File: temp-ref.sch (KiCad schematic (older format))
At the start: 37 parts, among them IC1 INA211AIDCKT, IC2 INA211AIDCKT, J1 Conn_01x05_Male, J2 USB_C_Receptacle_USB2.0, Q1 Q_NMOS_GDS, Q3 Q_NMOS_GDS, SW1 SW_SPST, SW2 SW_SPST, SW3 SW_SPST, SW4 SW_SPST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

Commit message: layout attempt 1
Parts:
- removed U6: adafruit-tft-120x135-4383, temp-ref:adafruit-tft-4383, symbol adafruit-tft-120x135-4383:adafruit-tft-120x135-4383
- added Q2: MMBT3904, Package_TO_SOT_SMD:SOT-23, symbol Transistor_BJT:MMBT3904
- added R3, R5: 10k, Resistor_SMD:R_0603_1608Metric, symbol Device:R_Small
- added R9: 33, Resistor_SMD:R_0603_1608Metric, symbol Device:R_Small
- added U6: spi-tft-1.14-240x135, temp-ref:TFT-1.14-240-135, symbol spi-tft-1.14:spi-tft-1.14-240x135
- J2: footprint Connector_USB:USB_C_Receptacle_JAE_DX07S024WJ3R400 -> Connector_USB:USB_C_Receptacle_Amphenol_12401610E4-2A
- SW1, SW2, SW3, SW4: footprint Button_Switch_SMD:SW_Push_1P1T_NO_CK_KSC7xxJ -> temp-ref:5.2mm_Tact_reverse_mount
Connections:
- net labels removed: DISP_MISO, DISP_SDCS
- wire segments 216 -> 231
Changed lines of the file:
@@
 F 0 "J2" H 6557 5367 50  0000 C CNN
 F 1 "USB_C_Receptacle_USB2.0" H 6557 5276 50  0000 C CNN
-F 2 "Connector_USB:USB_C_Receptacle_JAE_DX07S024WJ3R400" H 6600 4500 50  0001 C CNN
+F 2 "Connector_USB:USB_C_Receptacle_Amphenol_12401610E4-2A" H 6600 4500 50  0001 C CNN
 F 3 "https://www.usb.org/sites/default/files/documents/usb_type-c.zip" H 6600 4500 50  0001 C CNN
 	1    6450 4500
@@
 F 0 "SW1" H 7150 2485 50  0000 C CNN
 F 1 "SW_SPST" H 7150 2394 50  0000 C CNN
-F 2 "Button_Switch_SMD:SW_Push_1P1T_NO_CK_KSC7xxJ" H 7150 2250 50  0001 C CNN
+F 2 "temp-ref:5.2mm_Tact_reverse_mount" H 7150 2250 50  0001 C CNN
 F 3 "~" H 7150 2250 50  0001 C CNN
 	1    7150 2250
@@
 F 0 "SW2" H 7150 2935 50  0000 C CNN
 F 1 "SW_SPST" H 7150 2844 50  0000 C CNN
-F 2 "Button_Switch_SMD:SW_Push_1P1T_NO_CK_KSC7xxJ" H 7150 2700 50  0001 C CNN
+F 2 "temp-ref:5.2mm_Tact_reverse_mount" H 7150 2700 50  0001 C CNN
 F 3 "~" H 7150 2700 50  0001 C CNN
 	1    7150 2700
@@
 F 0 "SW3" H 7150 3335 50  0000 C CNN
 F 1 "SW_SPST" H 7150 3244 50  0000 C CNN
-F 2 "Button_Switch_SMD:SW_Push_1P1T_NO_CK_KSC7xxJ" H 7150 3100 50  0001 C CNN
+F 2 "temp-ref:5.2mm_Tact_reverse_mount" H 7150 3100 50  0001 C CNN
 F 3 "~" H 7150 3100 50  0001 C CNN
 	1    7150 3100
@@
 F 0 "SW4" H 7150 3585 50  0000 C CNN
 F 1 "SW_SPST" H 7150 3494 50  0000 C CNN
-F 2 "Button_Switch_SMD:SW_Push_1P1T_NO_CK_KSC7xxJ" H 7150 3350 50  0001 C CNN
+F 2 "temp-ref:5.2mm_Tact_reverse_mount" H 7150 3350 50  0001 C CNN
 F 3 "~" H 7150 3350 50  0001 C CNN
 	1    7150 3350
@@
 Text GLabel 1500 2000 0    50   Input ~ 0
 HEATER1
-Text GLabel 1500 3000 0    50   Input ~ 0
+Text GLabel 1500 2500 0    50   Input ~ 0
 WIFI_G0
-Text GLabel 1500 3100 0    50   Input ~ 0
+Text GLabel 1500 1800 0    50   Input ~ 0
 WIFI_G2
 Text GLabel 1500 2300 0    50   Input ~ 0
 WIFI_TX
-Text GLabel 1500 2900 0    50   Input ~ 0
+Text GLabel 1500 1700 0    50   Input ~ 0
 WIFI_RST
 Text GLabel 6800 2250 0    50   Input ~ 0
@@
 L power:+3V3 #PWR0149
 U 1 1 5EB7C07B
-P 4650 4500
-F 0 "#PWR0149" H 4650 4350 50  0001 C CNN
-F 1 "+3V3" H 4665 4673 50  0000 C CNN
-F 2 "" H 4650 4500 50  0001 C CNN
-F 3 "" H 4650 4500 50  0001 C CNN
-	1    4650 4500
-	0    -1   -1   0
-$EndComp
-Wire Wire Line
-	4800 4500 4650 4500
+P 4850 5950
+F 0 "#PWR0149" H 4850 5800 50  0001 C CNN
+F 1 "+3V3" H 4865 6123 50  0000 C CNN
+F 2 "" H 4850 5950 50  0001 C CNN
+F 3 "" H 4850 5950 50  0001 C CNN
+	1    4850 5950
+	0    -1   -1   0
+$EndComp
 $Comp
 L power:GND #PWR0150
 U 1 1 5EB87206
-P 4700 4700
-F 0 "#PWR0150" H 4700 4450 50  0001 C CNN
-F 1 "GND" H 4705 4527 50  0000 C CNN
-F 2 "" H 4700 4700 50  0001 C CNN
-F 3 "" H 4700 4700 50  0001 C CNN
-	1    4700 4700
+P 4800 6850
+F 0 "#PWR0150" H 4800 6600 50  0001 C CNN
+F 1 "GND" H 4805 6677 50  0000 C CNN
+F 2 "" H 4800 6850 50  0001 C CNN
+F 3 "" H 4800 6850 50  0001 C CNN
+	1    4800 6850
 	0    1    1    0
 $EndComp
-Wire Wire Line
-	4800 4700 4700 4700
-Text GLabel 4450 4800 0    50   Input ~ 0
+Text GLabel 4850 6450 0    50   Input ~ 0
 DISP_SCK
-Text GLabel 4450 4900 0    50   Input ~ 0
-DISP_MISO
-Text GLabel 4450 5000 0    50   Input ~ 0
+Text GLabel 4850 6350 0    50   Input ~ 0
 DISP_MOSI
-Text GLabel 4450 5100 0    50   Input ~ 0
+Text GLabel 4850 6550 0    50   Input ~ 0
 DISP_CS
-Text GLabel 4450 5200 0    50   Input ~ 0
+Text GLabel 4850 6150 0    50   Input ~ 0
 DISP_RST
-Text GLabel 4450 5300 0    50   Input ~ 0
+Text GLabel 4850 6250 0    50   Input ~ 0
 DISP_DC
-Text GLabel 4450 5400 0    50   Input ~ 0
-DISP_SDCS
-Text GLabel 4450 5500 0    50   Input ~ 0
+Text GLabel 3000 6350 0    50   Input ~ 0
 DISP_BACKLIGHT
-Wire Wire Line
-	4800 4800 4450 4800
-Wire Wire Line
-	4800 4900 4450 4900
-Wire Wire Line
-	4800 5000 4450 5000
-Wire Wire Line
-	4800 5100 4450 5100
-Wire Wire Line
-	4800 5200 4450 5200
-Wire Wire Line
-	4800 5300 4450 5300
-Wire Wire Line
-	4800 5400 4450 5400
-Wire Wire Line
-	4800 5500 4450 5500
 Text GLabel 1500 2400 0    50   Input ~ 0
 WIFI_RX
@@
 Text GLabel 3650 1700 2    50   Input ~ 0
 DISP_SCK
-Text GLabel 1500 2500 0    50   Input ~ 0
-DISP_MISO
 Text GLabel 3650 1800 2    50   Input ~ 0
 DISP_MOSI
@@
 Text GLabel 1500 4000 0    50   Input ~ 0
 DISP_DC
-Text GLabel 1500 1800 0    50   Input ~ 0
-DISP_SDCS
 Text GLabel 1500 2800 0    50   Input ~ 0
 DISP_BACKLIGHT
@@
 	9900 9300 9850 9300
 $Comp
-L adafruit-tft-120x135-4383:adafruit-tft-120x135-4383 U6
-U 1 1 5F0AA818
-P 4950 5800
-F 0 "U6" H 5228 6671 50  0000 L CNN
-F 1 "adafruit-tft-120x135-4383" H 5228 6580 50  0000 L CNN
-F 2 "temp-ref:adafruit-tft-4383" H 4950 5800 50  0001 C CNN
-F 3 "" H 4950 5800 50  0001 C CNN
-	1    4950 5800
-	1    0    0    -1
-$EndComp
-$Comp
 L STS-30-DIS:STS-30-DIS U5
 U 1 1 5F0AB74B
@@
 	0    -1   1    0
 $EndComp
+$Comp
+L spi-tft-1.14:spi-tft-1.14-240x135 U6
+U 1 1 5EAE6EF2
+P 5150 6750
+F 0 "U6" H 5378 7146 50  0000 L CNN
+F 1 "spi-tft-1.14-240x135" H 5378 7055 50  0000 L CNN
+F 2 "temp-ref:TFT-1.14-240-135" H 5250 6250 50  0001 C CNN
+F 3 "" H 5250 6250 50  0001 C CNN
+	1    5150 6750
+	1    0    0    -1
+$EndComp
+$Comp
+L Transistor_BJT:MMBT3904 Q2
+U 1 1 5EA5FD70
+P 3850 6350
+F 0 "Q2" H 4041 6396 50  0000 L CNN
+F 1 "MMBT3904" H 3500 6500 50  0000 L CNN
+F 2 "Package_TO_SOT_SMD:SOT-23" H 4050 6275 50  0001 L CIN
+F 3 "https://www.fairchildsemi.com/datasheets/2N/2N3904.pdf" H 3850 6350 50  0001 L CNN
+	1    3850 6350
+	1    0    0    -1
+$EndComp
+$Comp
+L Device:R_Small R5
+U 1 1 5EA60C2A
+P 3400 6350
+F 0 "R5" V 3350 6200 50  0000 C CNN
+F 1 "10k" V 3400 6350 39  0000 C CNN
+F 2 "Resistor_SMD:R_0603_1608Metric" H 3400 6350 50  0001 C CNN
+F 3 "~" H 3400 6350 50  0001 C CNN
+	1    3400 6350
+	0    -1   -1   0
+$EndComp
+$Comp
+L Device:R_Small R3
+U 1 1 5EA615A5
+P 3200 6150
+F 0 "R3" V 3150 6000 50  0000 C CNN
+F 1 "10k" V 3200 6150 39  0000 C CNN
+F 2 "Resistor_SMD:R_0603_1608Metric" H 3200 6150 50  0001 C CNN
+F 3 "~" H 3200 6150 50  0001 C CNN
+	1    3200 6150
+	1    0    0    -1
+$EndComp
+$Comp
+L power:+3V3 #PWR0152
+U 1 1 5EA61EE0
+P 3200 5950
+F 0 "#PWR0152" H 3200 5800 50  0001 C CNN
+F 1 "+3V3" H 3215 6123 50  0000 C CNN
+F 2 "" H 3200 5950 50  0001 C CNN
+F 3 "" H 3200 5950 50  0001 C CNN
+	1    3200 5950
+	1    0    0    -1
+$EndComp
+$Comp
+L Device:R_Small R9
+U 1 1 5EA71536
+P 4350 6050
+F 0 "R9" V 4300 5900 50  0000 C CNN
+F 1 "33" V 4350 6050 39  0000 C CNN
+F 2 "Resistor_SMD:R_0603_1608Metric" H 4350 6050 50  0001 C CNN
+F 3 "~" H 4350 6050 50  0001 C CNN
+	1    4350 6050
+	0    -1   -1   0
+$EndComp
+Wire Wire Line
+	4950 6050 4450 6050
+Wire Wire Line
+	4250 6050 3950 6050
+Wire Wire Line
+	3950 6050 3950 6150
+Wire Wire Line
+	4850 5950 4950 5950
+$Comp
+L power:GND #PWR0153
+U 1 1 5EA9D001
+P 3950 6600
+F 0 "#PWR0153" H 3950 6350 50  0001 C CNN
+F 1 "GND" H 3955 6427 50  0000 C CNN
+F 2 "" H 3950 6600 50  0001 C CNN
+F 3 "" H 3950 6600 50  0001 C CNN
+	1    3950 6600
+	1    0    0    -1
+$EndComp
+Wire Wire Line
+	3950 6550 3950 6600
+Wire Wire Line
+	3650 6350 3500 6350
+Wire Wire Line
+	3300 6350 3200 6350
+Wire Wire Line
+	3200 6250 3200 6350
+Connection ~ 3200 6350
+Wire Wire Line
+	3200 6350 3000 6350
+Wire Wire Line
+	3200 5950 3200 6050
+$Comp
+L power:+3V3 #PWR0154
+U 1 1 5EAE9DAC
+P 4550 6650
+F 0 "#PWR0154" H 4550 6500 50  0001 C CNN
+F 1 "+3V3" H 4565 6823 50  0000 C CNN
+F 2 "" H 4550 6650 50  0001 C CNN
+F 3 "" H 4550 6650 50  0001 C CNN
+	1    4550 6650
+	0    -1   -1   0
+$EndComp
+Wire Wire Line
+	4550 6650 4950 6650
+Wire Wire Line
+	4950 6750 4900 6750
+Wire Wire Line
+	4900 6750 4900 6850
+Wire Wire Line
+	4900 6850 4950 6850
+Wire Wire Line
+	4800 6850 4900 6850
+Connection ~ 4900 6850
+Wire Wire Line
+	4850 6150 4950 6150
+Wire Wire Line
+	4950 6250 4850 6250
+Wire Wire Line
+	4950 6350 4850 6350
+Wire Wire Line
+	4950 6450 4850 6450
+Wire Wire Line
+	4950 6550 4850 6550
+Wire Wire Line
+	1500 2300 1600 2300
+Wire Wire Line
+	1500 2400 1600 2400
+Wire Wire Line
+	1500 2500 1600 2500
+Wire Wire Line
+	1600 1800 1500 1800
+Wire Wire Line
+	1500 1700 1600 1700
 $EndSCHEMATC

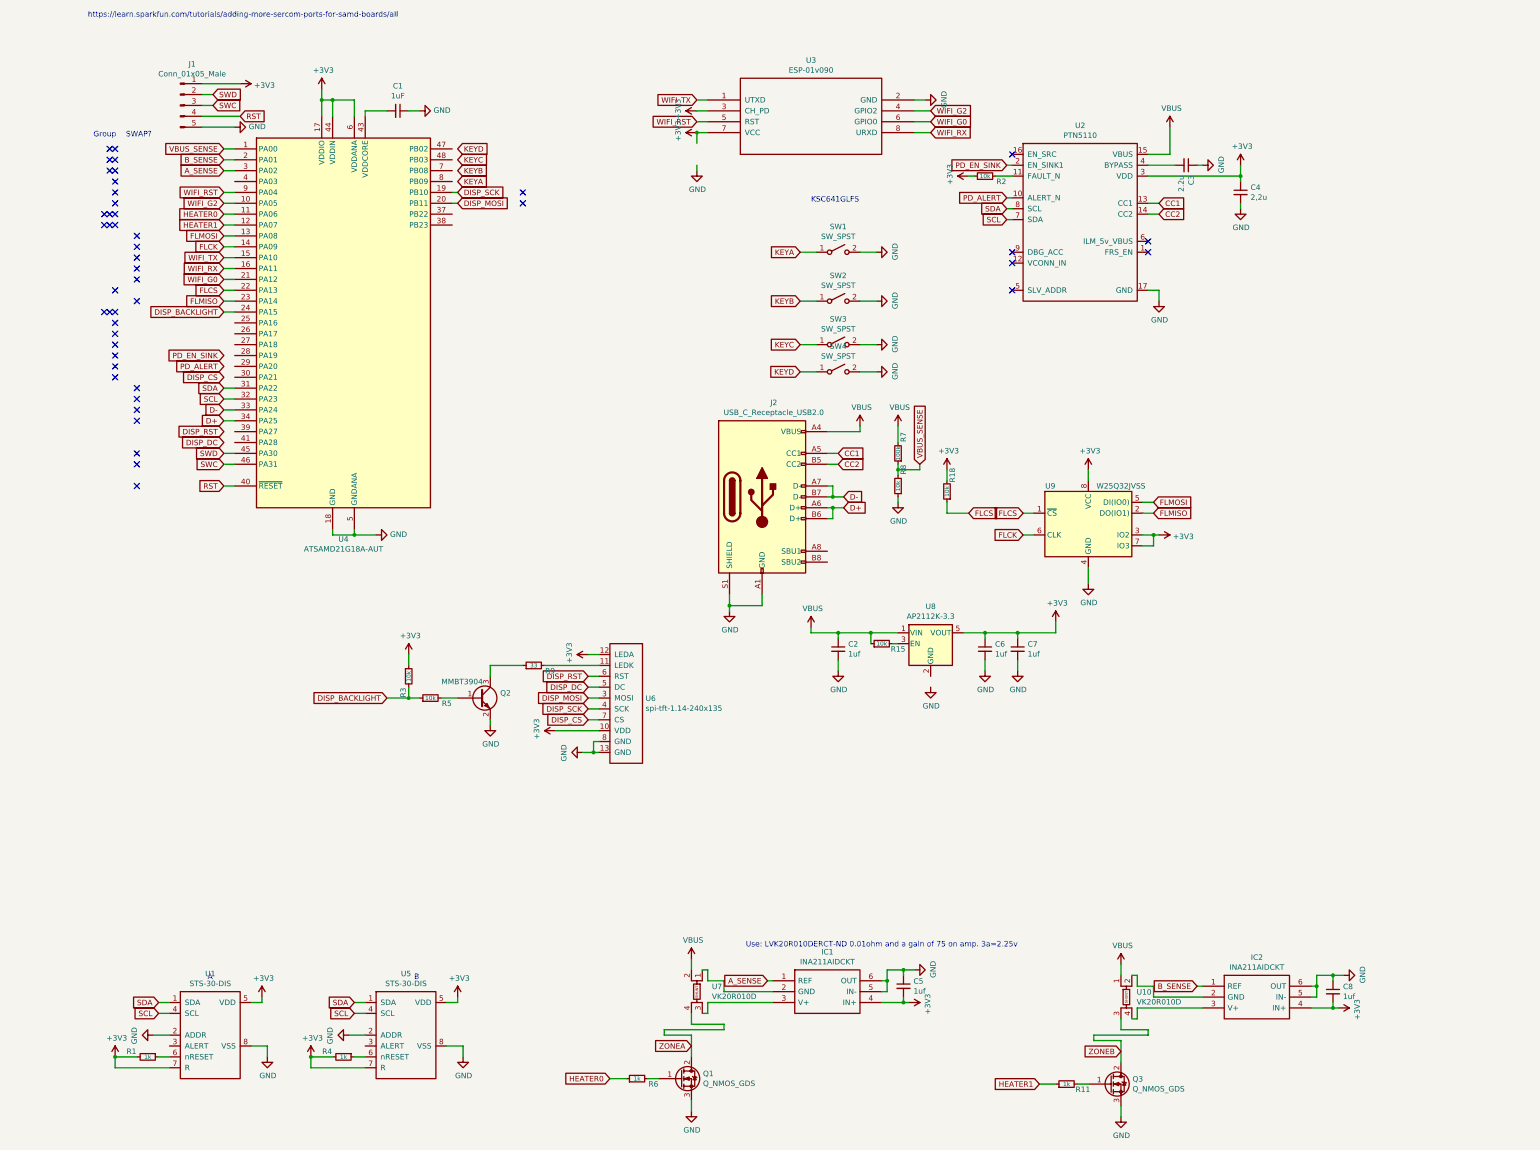
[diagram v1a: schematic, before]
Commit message: REworked electronics into smaller board. Heating elements will be seperate.
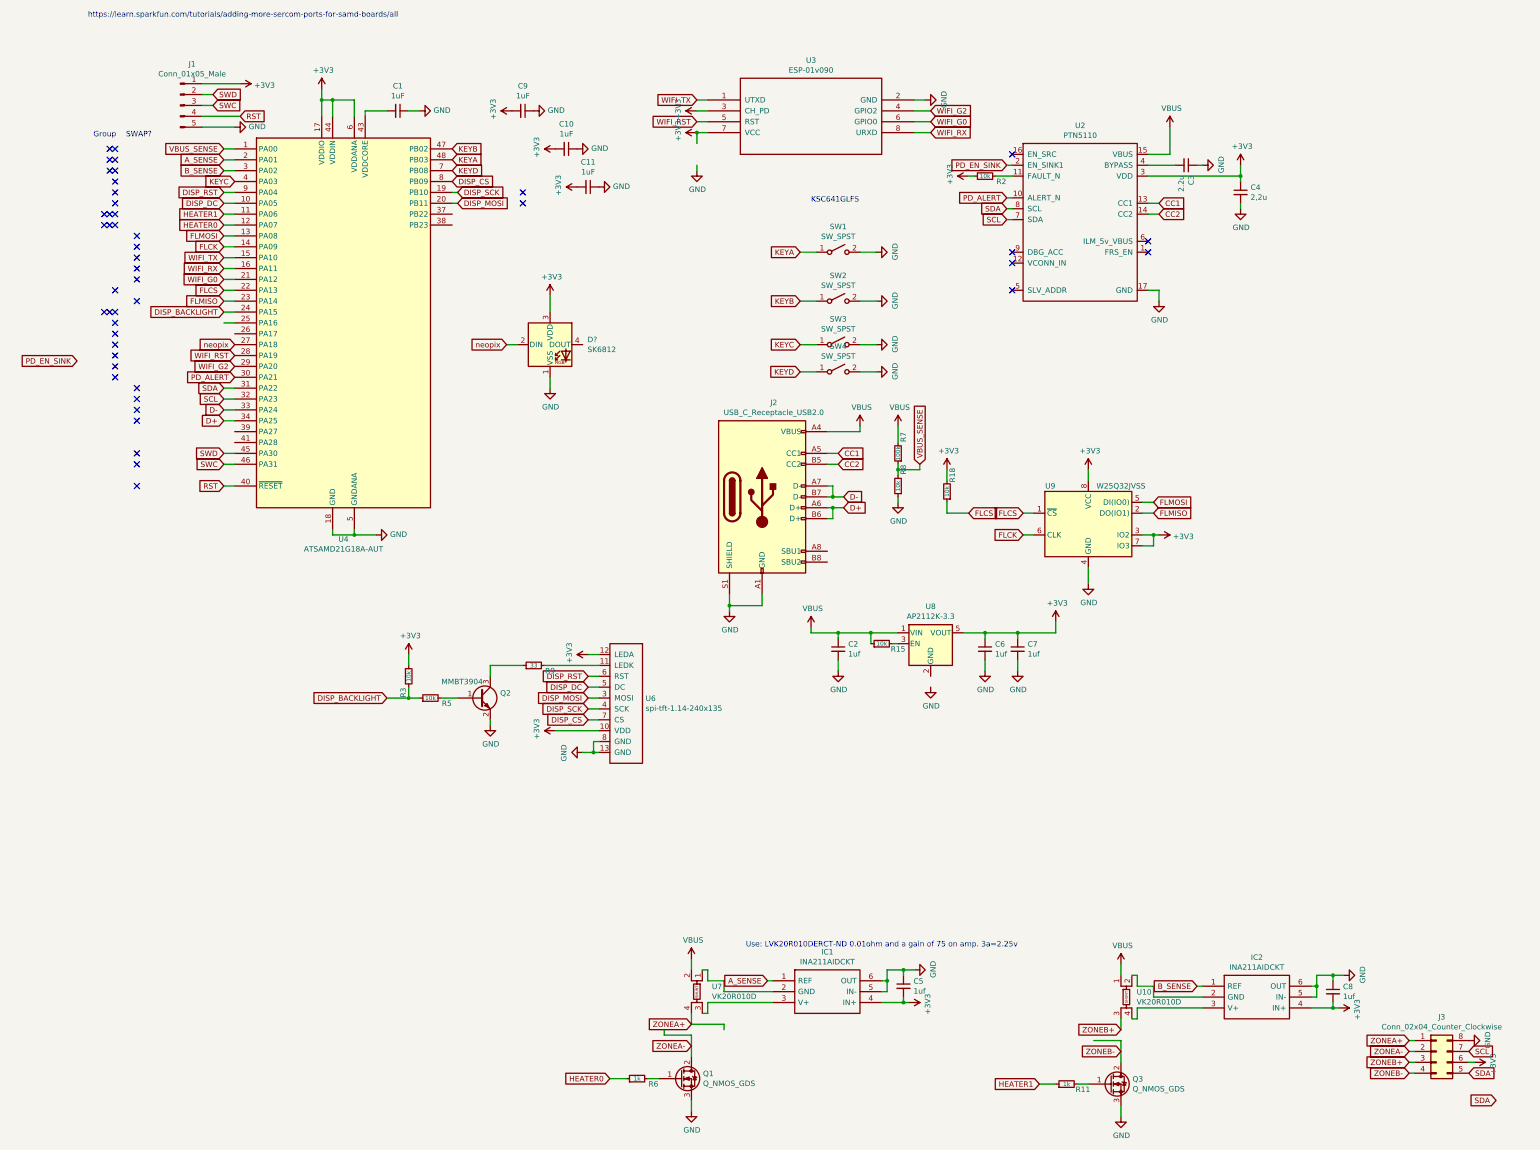
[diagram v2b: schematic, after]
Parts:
- removed R1, R4: 1k, Resistor_SMD:R_0603_1608Metric, symbol Device:R_Small
- removed U1, U5: STS-30-DIS, temp-ref:sts, symbol STS-30-DIS:STS-30-DIS
- added C10, C11, C9: 1uF, Capacitor_SMD:C_0603_1608Metric, symbol Device:C_Small
- added D?: SK6812, LED_SMD:LED_SK6812_PLCC4_5.0x5.0mm_P3.2mm, symbol LED:SK6812
- added J3: Conn_02x04_Counter_Clockwise, Connector_PinSocket_2.54mm:PinSocket_2x04_P2.54mm_Horizontal, symbol Connector_Generic:Conn_02x04_Counter_Clockwise
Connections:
- net +3V3: now also C10.2, C11.2, C9.2, D?.3 (VDD), J3.6 (Pin_6)
- net A_SENSE: now also U4.2 (PA01); no longer U4.3 (PA02)
- net B_SENSE: now also U4.3 (PA02); no longer U4.2 (PA01)
- net DISP_CS: now also U4.8 (PB09)
- net DISP_DC: now also U4.10 (PA05)
- net DISP_RST: now also U4.9 (PA04)
- net GND: now also C10.1, C11.1, C9.1, D?.1 (VSS), J3.8 (Pin_8)
- net HEATER0: now also U4.12 (PA07); no longer U4.11 (PA06)
- net HEATER1: now also U4.11 (PA06); no longer U4.12 (PA07)
- net KEYA: now also U4.48 (PB03)
- net KEYB: now also U4.47 (PB02)
- net KEYC: now also U4.4 (PA03)
- net KEYD: now also U4.7 (PB08)
- net PD_ALERT: now also U4.30 (PA21)
- net SCL: now also J3.7 (Pin_7)
- net SDA: now also J3.5 (Pin_5)
- net WIFI_G2: now also U4.29 (PA20); no longer U4.10 (PA05)
- net WIFI_RST: now also U4.28 (PA19); no longer U4.9 (PA04)
- net neopix: now reaches U4.27 (PA18)
- net neopix: now also D?.2 (DIN)
- net ZONEA renamed ZONEA+
- net ZONEA+: now also J3.1 (Pin_1); no longer Q1.2 (D)
- net ZONEB renamed ZONEB+
- net ZONEB+: now also J3.3 (Pin_3); no longer Q3.2 (D)
- new net ZONEA-: J3.2 (Pin_2), Q1.2 (D)
- new net ZONEB-: J3.4 (Pin_4), Q3.2 (D)
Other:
- note removed: "A\n"
- note removed: "B"
